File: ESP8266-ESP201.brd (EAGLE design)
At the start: 59.4 x 41.9 mm, 17 parts

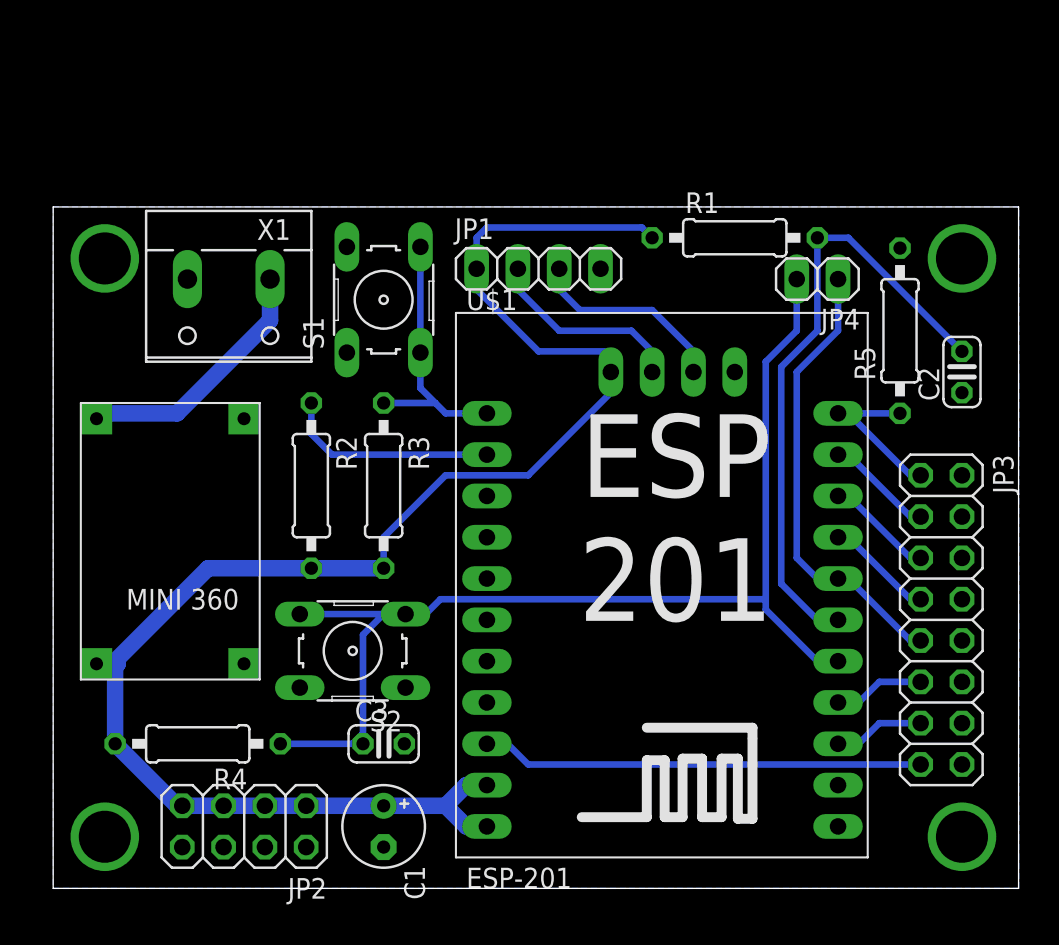
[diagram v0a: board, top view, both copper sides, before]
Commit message: New version of the board with proper mounting holes and smaller footprint
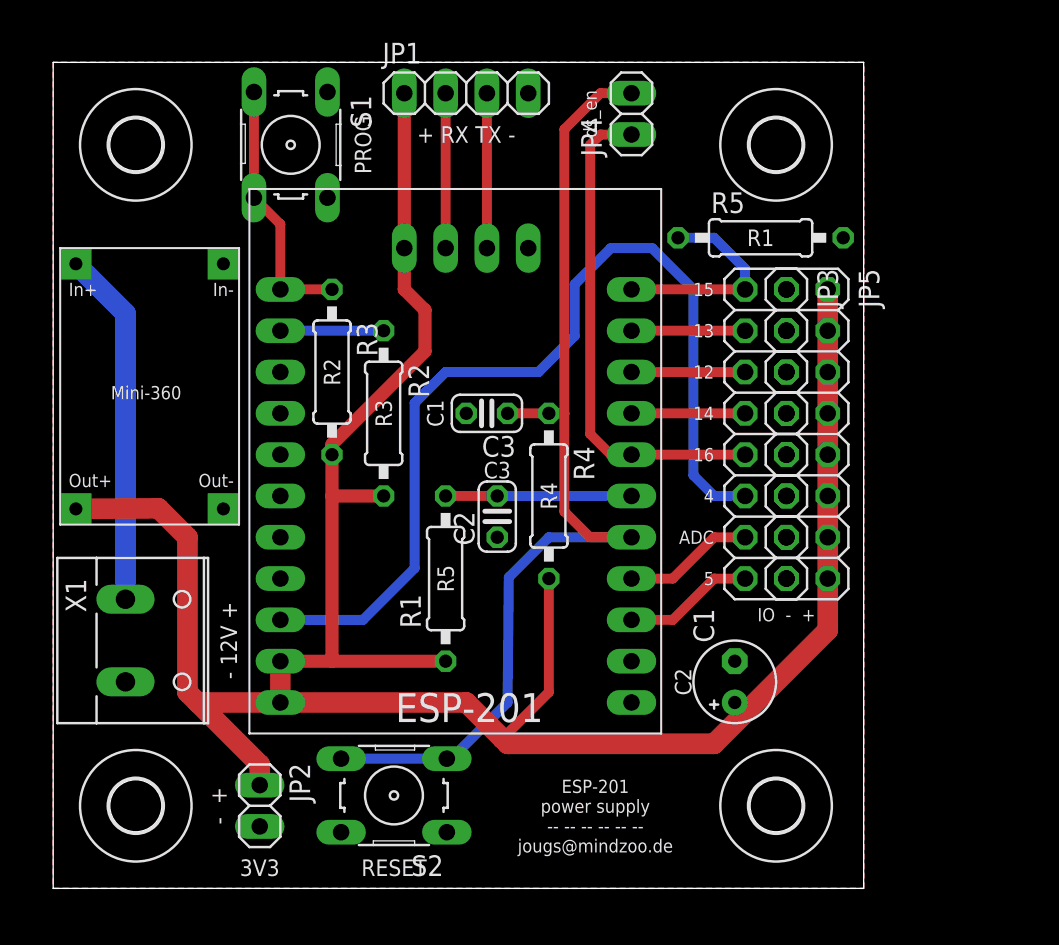
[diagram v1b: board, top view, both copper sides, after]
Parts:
- added H1, H2, H3, H4: MOUNT-HOLE3.2, holes:3,2
- added JP5: (no value), pinhead:2X08
- JP2: device pinhead:2X04 -> pinhead:1X02
- moved C2 29.9 mm to (27.3, 22.9)
- moved R1 27.5 mm to (24.1, 19.1), turned to 90 degrees
- moved R4 26.4 mm to (30.5, 24.1), turned to 270 degrees
- moved C1 23.3 mm to (41.9, 12.7), turned to 90 degrees
- moved X1 22.3 mm to (5.08, 15.2), turned to 270 degrees
- moved C3 21.3 mm to (26.7, 29.2), turned to 180 degrees
- moved JP3 15.7 mm to (43.8, 27.9)
- moved JP4 15.3 mm to (35.6, 47.6), turned to 90 degrees
- moved U$1 14.8 mm to (14.0, 11.4)
- moved JP1 11.7 mm to (25.4, 48.9)
- moved S1 11.1 mm to (14.6, 45.7), turned to 270 degrees
- moved R5 10.3 mm to (43.5, 40.0), turned to 0 degrees
- moved U$2 9.61 mm to (11.4, 39.4)
- moved S2 9.25 mm to (21.0, 5.71)
- moved R3 7.67 mm to (17.1, 31.8)
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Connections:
- net +3V3: now also JP5.10, JP5.12, JP5.14, JP5.16, JP5.2, JP5.4, JP5.6, JP5.8; no longer JP2.3, JP2.5, JP2.7
- net ADC: now also JP3.13; no longer JP3.11
- net GND: now also JP5.1, JP5.11, JP5.13, JP5.15, JP5.3, JP5.5, JP5.7, JP5.9; no longer JP2.4, JP2.6, JP2.8
- net GPIO4: now also JP3.11; no longer JP3.15
- net GPIO5: now also JP3.15; no longer JP3.13
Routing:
- net +3V3: track 102.7 -> 153.9 mm
- net GPIO4: track 27.2 -> 58.9 mm
- net CH_PD: track 38.4 -> 11.4 mm
- net GPIO2: track 13.2 -> 6.35 mm
- net +12V: track 15.7 -> 21.9 mm
- net RESET: track 69.7 -> 64.7 mm
- net TX: track 12.4 -> 9.53 mm
- net RX: track 12.4 -> 9.53 mm
- net GPIO16: track 27.9 -> 30.6 mm
- net GPIO15: track 10.5 -> 13.2 mm
- net GPIO5: track 5.61 -> 8.04 mm
- net ADC: track 5.61 -> 8.04 mm
- net GPIO0: track 16.6 -> 16.0 mm
- added copper zone on layer 1, net GND
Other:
- board size 59.4 x 41.9 mm -> 49.8 x 50.8 mm
- board text added: "+ RX TX -"
- board text added: "- +"
- board text added: "- 12V +"
- board text added: "12"
- board text added: "13"
- board text added: "14"
- board text added: "15"
- board text added: "16"
- board text added: "3V3"
- board text added: "4"
- board text added: "5"
- board text added: "ADC"
- board text added: "C1"
- board text added: "C2"
- board text added: "C3"
- board text added: "ESP-201 power supply -- -- -- -- -- -- jougs@mindzoo.de"
- board text added: "IO - +"
- board text added: "PROG"
- board text added: "R1"
- board text added: "R2"
- board text added: "R3"
- board text added: "R4"
- board text added: "R5"
- board text added: "RESET"
- board text added: "ds_en"

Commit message: More compact layout and added bottom silk screen
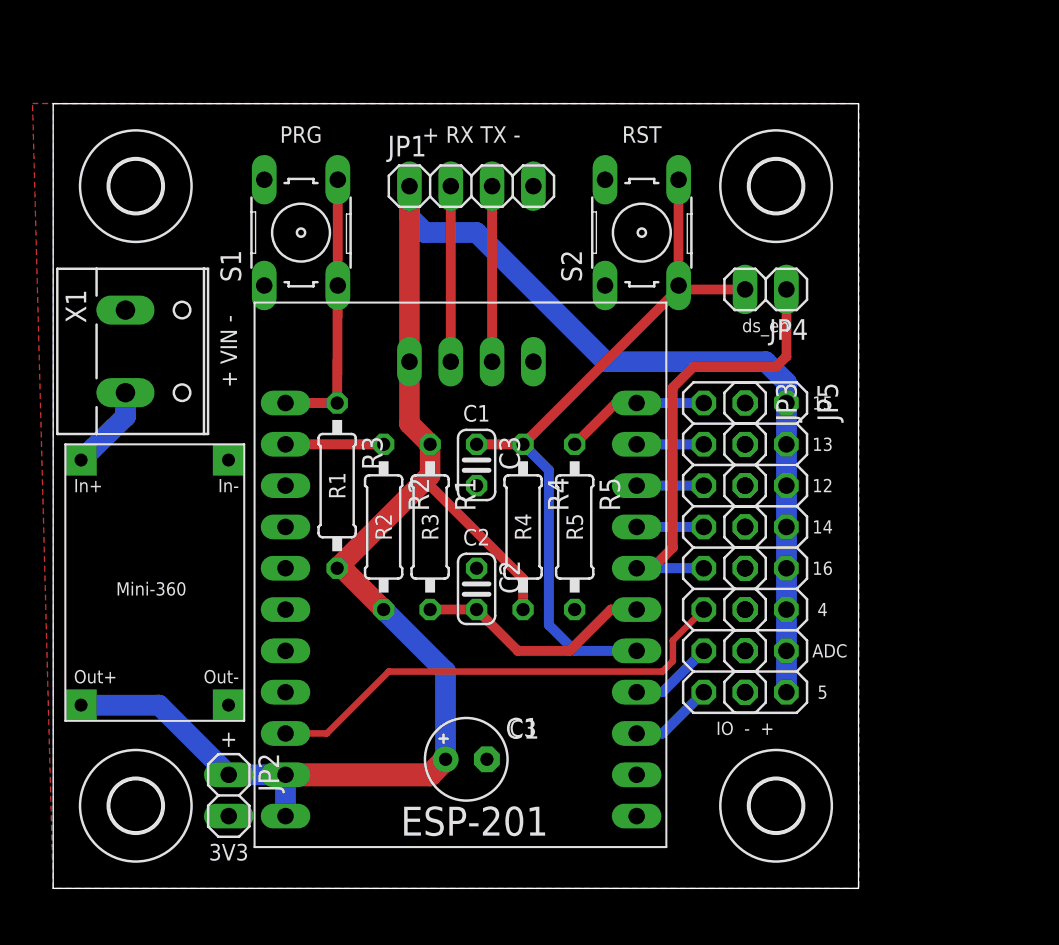
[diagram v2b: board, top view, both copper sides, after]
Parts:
- moved S2 37.8 mm to (36.2, 40.3), turned to 90 degrees
- moved R5 21.1 mm to (32.1, 22.2), turned to 270 degrees
- moved X1 17.8 mm to (5.08, 33.0)
- moved C1 17.2 mm to (25.4, 7.94), turned to 0 degrees
- moved JP4 13.6 mm to (43.8, 36.8), turned to 180 degrees
- moved U$2 12.1 mm to (11.7, 27.3)
- moved JP3 7.43 mm to (41.3, 21.0)
- moved JP5 7.43 mm to (43.8, 21.0)
- moved R3 6.99 mm to (17.5, 24.8)
- moved U$1 6.99 mm to (14.3, 4.45)
- moved R2 6.98 mm to (20.3, 22.2)
- moved JP1 5.72 mm to (25.7, 43.2)
- moved S1 5.43 mm to (15.2, 40.3), turned to 90 degrees
- moved C2 4.62 mm to (26.0, 18.4), turned to 270 degrees
- moved R1 3.31 mm to (23.2, 22.2), turned to 270 degrees
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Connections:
- net +12V: now also X1.2; no longer X1.1
- net GND: now also X1.1; no longer X1.2
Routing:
- net GPIO4: track 58.9 -> 29.6 mm
- net +3V3: track 153.9 -> 127.0 mm
- net RESET: track 64.7 -> 45.1 mm
- net +12V: track 21.9 -> 5.29 mm
- net GPIO15: track 13.2 -> 8.99 mm
- net CH_PD: track 11.4 -> 14.8 mm
- net GPIO5: track 8.04 -> 5.18 mm
- net GPIO14: track 6.98 -> 4.13 mm
- net GPIO13: track 6.98 -> 4.13 mm
- net GPIO12: track 6.98 -> 4.13 mm
- net ADC: track 8.04 -> 5.18 mm
- net GPIO16: track 30.6 -> 28.6 mm
- net TX: track 9.53 -> 10.8 mm
- net RX: track 9.53 -> 10.8 mm
- net GPIO0: track 16.0 -> 17.3 mm
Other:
- board size 49.8 x 50.8 mm -> 49.5 x 48.2 mm
- board text added: "+"
- board text added: "+ VIN -"
- board text added: "Adjust 3V3 before inserting module!"
- board text added: "ESP-201 base board v1.0"
- board text added: "PRG"
- board text added: "R1-R5: 3k3 C1+C2: 100n C3: 330µ VIN: 5..23V"
- board text added: "RST"
- board text added: "jougs@mindzoo.de"
- board text removed: "- +"
- board text removed: "- 12V +"
- board text removed: "ESP-201 power supply -- -- -- -- -- -- jougs@mindzoo.de"
- board text removed: "PROG"
- board text removed: "RESET"

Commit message: Increased size of 3v3 trace and updated GERBER files
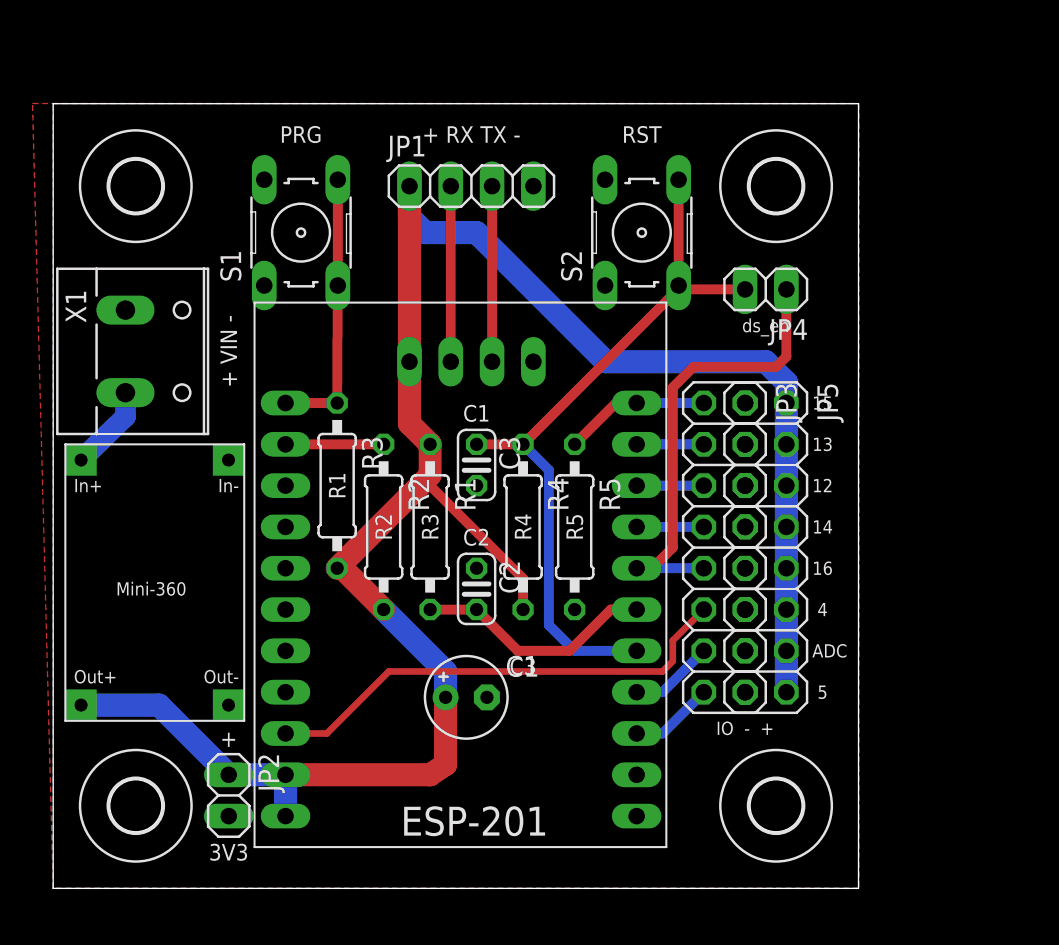
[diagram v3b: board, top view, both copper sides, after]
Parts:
- moved C1 3.81 mm to (25.4, 11.7)
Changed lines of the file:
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@@
 <text x="32.0675" y="22.225" size="1.016" layer="21" font="vector" rot="R90" align="center">R5</text>
 <text x="28.8925" y="22.225" size="1.016" layer="21" font="vector" rot="R90" align="center">R4</text>
-<text x="28.8925" y="9.8425" size="1.016" layer="21" font="vector" align="center">C3</text>
+<text x="28.8925" y="13.6525" size="1.016" layer="21" font="vector" align="center">C3</text>
 <text x="26.035" y="29.21" size="1.016" layer="21" font="vector" align="center">C1</text>
 <text x="26.035" y="21.59" size="1.016" layer="21" font="vector" rot="R180" align="center">C2</text>
@@
 </element>
 <element name="R1" library="resistor" package="0207/10" value="" x="23.1775" y="22.225" rot="R270"/>
-<element name="C1" library="resistor" package="E2,5-5" value="" x="25.4" y="7.9375" smashed="yes">
-<attribute name="NAME" x="27.813" y="9.2075" size="1.27" layer="25" ratio="10"/>
-<attribute name="VALUE" x="27.813" y="5.5245" size="1.27" layer="27" ratio="10"/>
+<element name="C1" library="resistor" package="E2,5-5" value="" x="25.4" y="11.7475" smashed="yes">
+<attribute name="NAME" x="27.813" y="13.0175" size="1.27" layer="25" ratio="10"/>
+<attribute name="VALUE" x="27.813" y="9.3345" size="1.27" layer="27" ratio="10"/>
 </element>
 <element name="R2" library="resistor" package="0207/10" value="" x="20.32" y="22.225" rot="R270"/>
@@
 <contactref element="JP5" pad="12"/>
 <contactref element="JP5" pad="14"/>
-<wire x1="14.2875" y1="6.985" x2="14.2875" y2="4.445" width="1.27" layer="16"/>
-<wire x1="45.085" y1="29.845" x2="45.085" y2="27.305" width="1.27" layer="16"/>
-<wire x1="45.085" y1="27.305" x2="45.085" y2="24.765" width="1.27" layer="16"/>
-<wire x1="45.085" y1="24.765" x2="45.085" y2="22.225" width="1.27" layer="16"/>
-<wire x1="45.085" y1="22.225" x2="45.085" y2="19.685" width="1.27" layer="16"/>
-<wire x1="45.085" y1="19.685" x2="45.085" y2="17.145" width="1.27" layer="16"/>
-<wire x1="45.085" y1="17.145" x2="45.085" y2="14.605" width="1.27" layer="16"/>
-<wire x1="45.085" y1="14.605" x2="45.085" y2="12.065" width="1.27" layer="16"/>
-<wire x1="1.712696875" y1="11.270209375" x2="6.509790625" y2="11.270209375" width="1.27" layer="16"/>
-<wire x1="6.509790625" y1="11.270209375" x2="10.795" y2="6.985" width="1.27" layer="16"/>
-<wire x1="10.795" y1="6.985" x2="14.2875" y2="6.985" width="1.27" layer="16"/>
+<wire x1="14.2875" y1="6.985" x2="14.2875" y2="4.445" width="1.4224" layer="16"/>
+<wire x1="45.085" y1="29.845" x2="45.085" y2="27.305" width="1.4224" layer="16"/>
+<wire x1="45.085" y1="27.305" x2="45.085" y2="24.765" width="1.4224" layer="16"/>
+<wire x1="45.085" y1="24.765" x2="45.085" y2="22.225" width="1.4224" layer="16"/>
+<wire x1="45.085" y1="22.225" x2="45.085" y2="19.685" width="1.4224" layer="16"/>
+<wire x1="45.085" y1="19.685" x2="45.085" y2="17.145" width="1.4224" layer="16"/>
+<wire x1="45.085" y1="17.145" x2="45.085" y2="14.605" width="1.4224" layer="16"/>
+<wire x1="45.085" y1="14.605" x2="45.085" y2="12.065" width="1.4224" layer="16"/>
+<wire x1="1.712696875" y1="11.270209375" x2="6.509790625" y2="11.270209375" width="1.4224" layer="16"/>
+<wire x1="6.509790625" y1="11.270209375" x2="10.795" y2="6.985" width="1.4224" layer="16"/>
+<wire x1="10.795" y1="6.985" x2="14.2875" y2="6.985" width="1.4224" layer="16"/>
 <wire x1="14.2875" y1="6.985" x2="23.1775" y2="6.985" width="1.4224" layer="1"/>
-<wire x1="23.1775" y1="6.985" x2="24.13" y2="7.9375" width="1.4224" layer="1"/>
-<wire x1="24.13" y1="7.9375" x2="24.13" y2="13.335" width="1.27" layer="16"/>
-<wire x1="24.13" y1="13.335" x2="20.32" y2="17.145" width="1.27" layer="16"/>
+<wire x1="23.1775" y1="6.985" x2="24.13" y2="7.62" width="1.4224" layer="1"/>
+<wire x1="24.13" y1="7.62" x2="24.13" y2="11.7475" width="1.4224" layer="1"/>
+<wire x1="24.13" y1="11.7475" x2="24.13" y2="13.335" width="1.4224" layer="16"/>
+<wire x1="24.13" y1="13.335" x2="20.32" y2="17.145" width="1.4224" layer="16"/>
 <wire x1="17.4625" y1="19.685" x2="17.78" y2="19.685" width="0.6096" layer="1"/>
-<wire x1="17.78" y1="19.685" x2="20.32" y2="17.145" width="1.27" layer="1"/>
-<wire x1="23.1775" y1="27.305" x2="23.1775" y2="25.4" width="1.27" layer="1"/>
+<wire x1="17.78" y1="19.685" x2="20.32" y2="17.145" width="1.4224" layer="1"/>
+<wire x1="23.1775" y1="27.305" x2="23.1775" y2="25.4" width="1.4224" layer="1"/>
 <wire x1="23.1775" y1="25.4" x2="22.86" y2="25.0825" width="1.27" layer="1"/>
-<wire x1="22.86" y1="25.0825" x2="17.4625" y2="19.685" width="1.27" layer="1"/>
-<wire x1="21.9075" y1="32.385" x2="21.9075" y2="28.575" width="1.27" layer="1"/>
-<wire x1="21.9075" y1="28.575" x2="23.1775" y2="27.305" width="1.27" layer="1"/>
-<wire x1="21.9075" y1="43.18" x2="21.9075" y2="32.385" width="1.27" layer="1"/>
+<wire x1="22.86" y1="25.0825" x2="17.4625" y2="19.685" width="1.4224" layer="1"/>
+<wire x1="21.9075" y1="32.385" x2="21.9075" y2="28.575" width="1.4224" layer="1"/>
+<wire x1="21.9075" y1="28.575" x2="23.1775" y2="27.305" width="1.4224" layer="1"/>
+<wire x1="21.9075" y1="43.18" x2="21.9075" y2="32.385" width="1.4224" layer="1"/>
 <wire x1="28.8925" y1="17.145" x2="28.8925" y2="19.05" width="0.6096" layer="1"/>
 <wire x1="28.8925" y1="19.05" x2="22.86" y2="25.0825" width="0.6096" layer="1"/>
-<wire x1="45.085" y1="31.115" x2="43.815" y2="32.385" width="1.27" layer="16"/>
-<wire x1="43.815" y1="32.385" x2="33.9725" y2="32.385" width="1.27" layer="16"/>
-<wire x1="33.9725" y1="32.385" x2="26.035" y2="40.3225" width="1.27" layer="16"/>
-<wire x1="26.035" y1="40.3225" x2="22.86" y2="40.3225" width="1.27" layer="16"/>
-<wire x1="22.86" y1="40.3225" x2="21.9075" y2="41.275" width="1.27" layer="16"/>
-<wire x1="21.9075" y1="41.275" x2="21.9075" y2="43.18" width="1.27" layer="16"/>
-<wire x1="45.085" y1="31.115" x2="45.085" y2="29.845" width="1.27" layer="16"/>
+<wire x1="45.085" y1="31.115" x2="43.815" y2="32.385" width="1.4224" layer="16"/>
+<wire x1="43.815" y1="32.385" x2="33.9725" y2="32.385" width="1.4224" layer="16"/>
+<wire x1="33.9725" y1="32.385" x2="26.035" y2="40.3225" width="1.4224" layer="16"/>
+<wire x1="26.035" y1="40.3225" x2="22.86" y2="40.3225" width="1.4224" layer="16"/>
+<wire x1="22.86" y1="40.3225" x2="21.9075" y2="41.275" width="1.4224" layer="16"/>
+<wire x1="21.9075" y1="41.275" x2="21.9075" y2="43.18" width="1.4224" layer="16"/>
+<wire x1="45.085" y1="31.115" x2="45.085" y2="29.845" width="1.4224" layer="16"/>
 </signal>
 <signal name="TX">

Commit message: Removed 3V3 test point
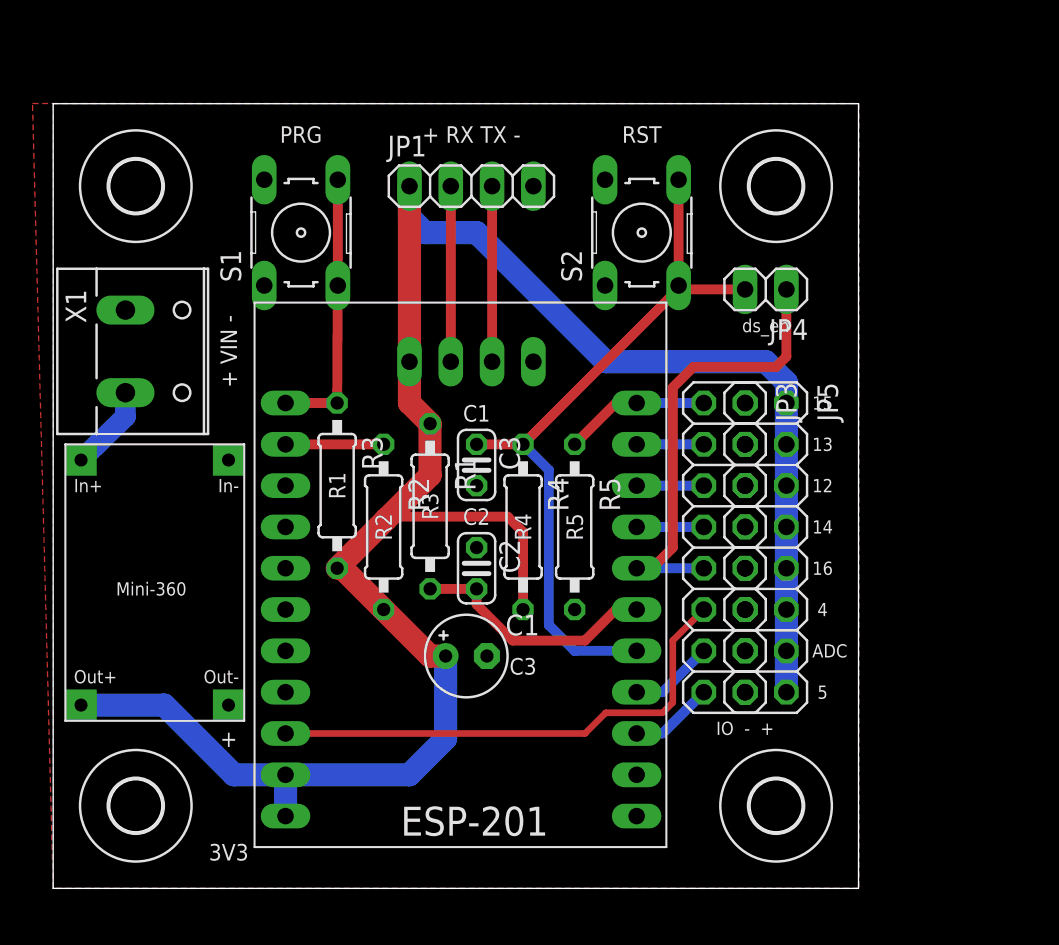
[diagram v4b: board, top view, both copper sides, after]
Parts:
- removed JP2: (no value), pinhead:1X02
- moved C1 2.54 mm to (25.4, 14.3)
- moved C2 1.27 mm to (26.0, 19.7)
- moved R1 1.27 mm to (23.2, 23.5)
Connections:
- net +3V3: no longer JP2.1
- net GND: no longer JP2.2
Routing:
- net +3V3: track 127.1 -> 130.0 mm
- net GPIO4: track 29.6 -> 31.1 mm
- net CH_PD: track 14.8 -> 15.4 mm
